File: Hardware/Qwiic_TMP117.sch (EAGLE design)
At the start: 21 parts, among them J1 PTH, U2 TMP117

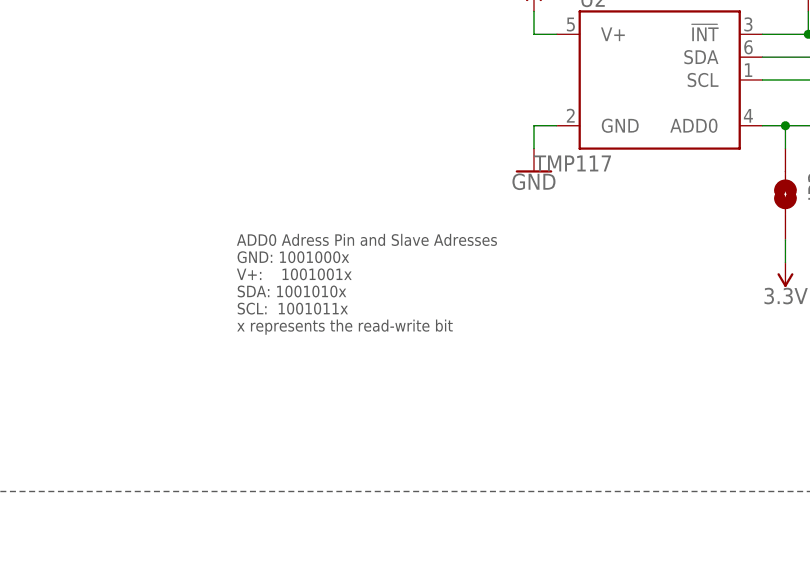
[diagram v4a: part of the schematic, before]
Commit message: Updated PCB
PCB updated to meet the jlcpcb specs with new milling width
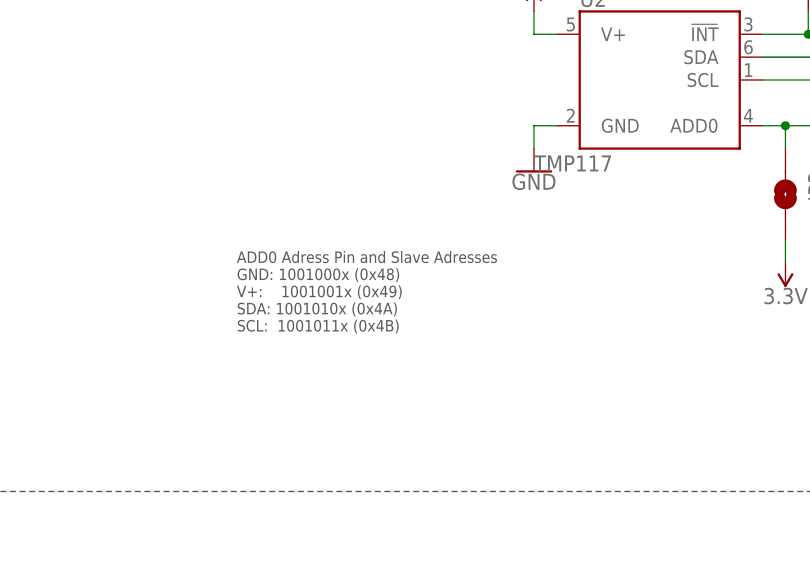
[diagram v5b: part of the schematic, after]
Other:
- note added: "ADD0 Adress Pin and Slave Adresses GND: 1001000x (0x48) V+: 1001001x (0x49) SDA: 1001010x (0x4A) SCL: 1001011x (0x4B)"
- note removed: "ADD0 Adress Pin and Slave Adresses GND: 1001000x V+: 1001001x SDA: 1001010x SCL: 1001011x x represents the read-write bit"
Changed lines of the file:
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@@
 pull-up from INT</text>
 <text x="104.14" y="114.3" size="1.27" layer="97">ADD0 Adress Pin and Slave Adresses
-GND: 1001000x
-V+:    1001001x
-SDA: 1001010x
-SCL:  1001011x
-x represents the read-write bit</text>
+GND: 1001000x (0x48)
+V+:    1001001x (0x49)
+SDA: 1001010x (0x4A)
+SCL:  1001011x (0x4B)</text>
 </plain>
 <instances>
